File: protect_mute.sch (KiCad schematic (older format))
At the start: 40 parts, among them K1 G5LE-1, K2 G5LE-1, Q1 BC546, Q2 BC556, Q3 BC546, Q4 BD140

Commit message: Opened on home office computer. Some rescue and lib conversion happened. Need to confirm no changes on work laptop.
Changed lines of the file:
@@
 EESchema Schematic File Version 4
-LIBS:AAMB-cache
 EELAYER 30 0
 EELAYER END
@@
 	1650 2925 1550 2925
 $Comp
-L Power-amp:+35V #PWR04
+L AAMB-rescue:+35V-Power-amp #PWR04
 U 1 1 5E273D13
 P 1800 1525

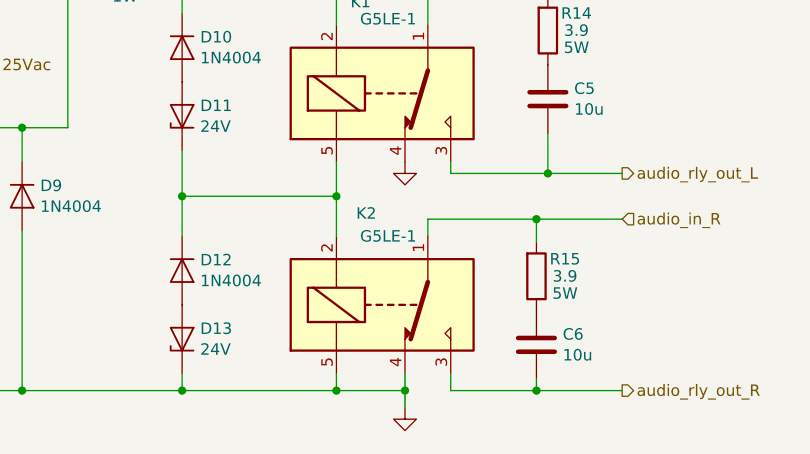
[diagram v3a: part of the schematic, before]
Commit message: Fixed several DRC errors. Tied audoi input returns to GND. Added Switch logic.
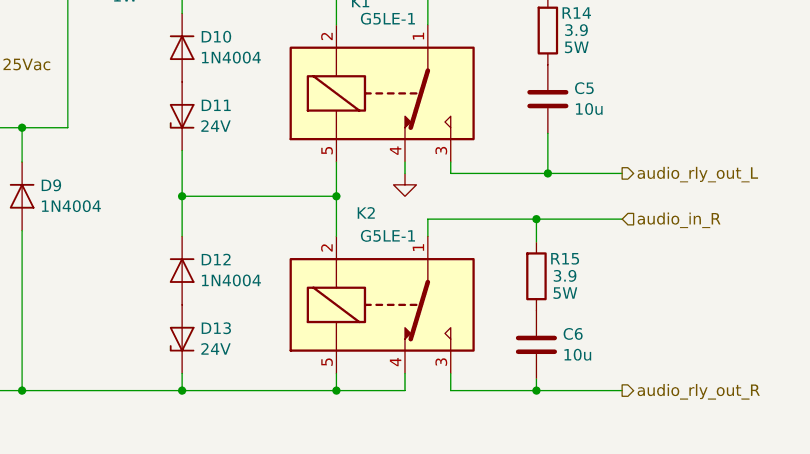
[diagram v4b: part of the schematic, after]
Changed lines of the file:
@@
 EESchema Schematic File Version 4
+LIBS:AAMB-cache
 EELAYER 30 0
 EELAYER END
@@
 L power:GND #PWR05
 U 1 1 5E3BFF33
-P 7400 3125
-F 0 "#PWR05" H 7400 2875 50  0001 C CNN
-F 1 "GND" H 7500 3000 50  0001 C CNN
-F 2 "" H 7400 3125 50  0001 C CNN
-F 3 "" H 7400 3125 50  0001 C CNN
-	1    7400 3125
+P 7400 3175
+F 0 "#PWR05" H 7400 2925 50  0001 C CNN
+F 1 "GND" H 7500 3050 50  0001 C CNN
+F 2 "" H 7400 3175 50  0001 C CNN
+F 3 "" H 7400 3175 50  0001 C CNN
+	1    7400 3175
 	1    0    0    -1
 $EndComp
@@
 	6325 2300 6425 2300
 Connection ~ 6425 2300
-$Comp
-L power:GND #PWR06
-U 1 1 5E3E6C3E
-P 7400 4200
-F 0 "#PWR06" H 7400 3950 50  0001 C CNN
-F 1 "GND" H 7475 4050 50  0001 C CNN
-F 2 "" H 7400 4200 50  0001 C CNN
-F 3 "" H 7400 4200 50  0001 C CNN
-	1    7400 4200
-	1    0    0    -1
-$EndComp
-Connection ~ 7400 4125
-Wire Wire Line
-	7400 4200 7400 4125
 Wire Wire Line
 	7600 3125 7600 3175
@@
 Text Label 6625 2300 0    50   ~ 0
 RLY+_L
+Wire Wire Line
+	7400 3175 7400 3125
 $EndSCHEMATC

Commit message: Schecmatic cleanup.
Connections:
- net RLY_-L_+R: now reaches D11.1 (K), D12.1 (K), K1.5, K2.2
- net RLY+_L renamed RLY_+L
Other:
- moved on the sheet: C1, C2, C3, C4, C5, C6, D1, D10, D11, D12, D13, D2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

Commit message: Cleaning up user configs.
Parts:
- C1, C2, C5, C6: footprint (none) -> Capacitor_SMD:C_1206_3216Metric_Pad1.42x1.75mm_HandSolder; DigiKey (none) -> https://www.digikey.com/product-detail/en/murata-electronic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
- C3, C4: footprint (none) -> Capacitor_THT:CP_Radial_D5.0mm_P2.00mm
- D11, D13: footprint (none) -> Diode_SMD:D_SMA
- R1, R10, R11, R12, R2, R3, R4, R5, R6, R7, R8, R9: footprint (none) -> Resistor_SMD:R_0603_1608Metric_Pad1.05x0.95mm_HandSolder
- R13: DigiKey (none) -> https://www.digikey.com/product-detail/en/yageo/FMP100JR-52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
- R14, R15: DigiKey (none) -> https://www.digikey.com/product-detail/en/vishay-bc-compone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
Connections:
- net audio_rly_out_L: now also C6.2; no longer C5.2
- net audio_rly_out_R: now also C5.2; no longer C6.2
- net at R15.1: now also C5.1; no longer C6.1
- net at R14.1: now also C6.1; no longer C5.1
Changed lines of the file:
@@
 F 0 "C4" H 5868 4746 50  0000 L CNN
 F 1 "1u" H 5868 4655 50  0000 L CNN
-F 2 "" H 5788 4550 50  0001 C CNN
+F 2 "Capacitor_THT:CP_Radial_D5.0mm_P2.00mm" H 5788 4550 50  0001 C CNN
 F 3 "~" H 5750 4700 50  0001 C CNN
 	1    5750 4700
@@
 F 0 "R12" V 5743 3525 50  0000 C CNN
 F 1 "100k" V 5834 3525 50  0000 C CNN
-F 2 "" V 5880 3525 50  0001 C CNN
+F 2 "Resistor_SMD:R_0603_1608Metric_Pad1.05x0.95mm_HandSolder" V 5880 3525 50  0001 C CNN
 F 3 "~" H 5950 3525 50  0001 C CNN
 	1    5950 3525
@@
 F 0 "R11" H 5370 4171 50  0000 L CNN
 F 1 "10k" H 5370 4080 50  0000 L CNN
-F 2 "" V 5230 4125 50  0001 C CNN
+F 2 "Resistor_SMD:R_0603_1608Metric_Pad1.05x0.95mm_HandSolder" V 5230 4125 50  0001 C CNN
 F 3 "~" H 5300 4125 50  0001 C CNN
 	1    5300 4125
@@
 F 0 "R10" V 4818 4425 50  0000 C CNN
 F 1 "10k" V 4909 4425 50  0000 C CNN
-F 2 "" V 4955 4425 50  0001 C CNN
+F 2 "Resistor_SMD:R_0603_1608Metric_Pad1.05x0.95mm_HandSolder" V 4955 4425 50  0001 C CNN
 F 3 "~" H 5025 4425 50  0001 C CNN
 	1    5025 4425
@@
 F 0 "R9" H 4480 3504 50  0000 R CNN
 F 1 "10k" H 4480 3595 50  0000 R CNN
-F 2 "" V 4480 3550 50  0001 C CNN
+F 2 "Resistor_SMD:R_0603_1608Metric_Pad1.05x0.95mm_HandSolder" V 4480 3550 50  0001 C CNN
 F 3 "~" H 4550 3550 50  0001 C CNN
 	1    4550 3550
@@
 F 0 "R8" H 3855 3504 50  0000 R CNN
 F 1 "100k" H 3855 3595 50  0000 R CNN
-F 2 "" V 3855 3550 50  0001 C CNN
+F 2 "Resistor_SMD:R_0603_1608Metric_Pad1.05x0.95mm_HandSolder" V 3855 3550 50  0001 C CNN
 F 3 "~" H 3925 3550 50  0001 C CNN
 	1    3925 3550
@@
 F 0 "R5" H 3330 3504 50  0000 R CNN
 F 1 "22k" H 3330 3595 50  0000 R CNN
-F 2 "" V 3330 3550 50  0001 C CNN
+F 2 "Resistor_SMD:R_0603_1608Metric_Pad1.05x0.95mm_HandSolder" V 3330 3550 50  0001 C CNN
 F 3 "~" H 3400 3550 50  0001 C CNN
 	1    3400 3550
@@
 F 0 "R4" H 3005 2679 50  0000 R CNN
 F 1 "100k" H 3005 2770 50  0000 R CNN
-F 2 "" V 3005 2725 50  0001 C CNN
+F 2 "Resistor_SMD:R_0603_1608Metric_Pad1.05x0.95mm_HandSolder" V 3005 2725 50  0001 C CNN
 F 3 "~" H 3075 2725 50  0001 C CNN
 	1    3075 2725
@@
 F 0 "R7" H 3855 2679 50  0000 R CNN
 F 1 "100k" H 3855 2770 50  0000 R CNN
-F 2 "" V 3855 2725 50  0001 C CNN
+F 2 "Resistor_SMD:R_0603_1608Metric_Pad1.05x0.95mm_HandSolder" V 3855 2725 50  0001 C CNN
 F 3 "~" H 3925 2725 50  0001 C CNN
 	1    3925 2725
@@
 F 0 "R6" H 3505 4679 50  0000 R CNN
 F 1 "22k" H 3505 4770 50  0000 R CNN
-F 2 "" V 3505 4725 50  0001 C CNN
+F 2 "Resistor_SMD:R_0603_1608Metric_Pad1.05x0.95mm_HandSolder" V 3505 4725 50  0001 C CNN
 F 3 "~" H 3575 4725 50  0001 C CNN
 	1    3575 4725
@@
 F 0 "R1" V 2182 3750 50  0000 C CNN
 F 1 "100k" V 2091 3750 50  0000 C CNN
-F 2 "" V 1905 3750 50  0001 C CNN
+F 2 "Resistor_SMD:R_0603_1608Metric_Pad1.05x0.95mm_HandSolder" V 1905 3750 50  0001 C CNN
 F 3 "~" H 1975 3750 50  0001 C CNN
 	1    1975 3750
@@
 F 0 "R2" V 2182 4500 50  0000 C CNN
 F 1 "100k" V 2091 4500 50  0000 C CNN
-F 2 "" V 1905 4500 50  0001 C CNN
+F 2 "Resistor_SMD:R_0603_1608Metric_Pad1.05x0.95mm_HandSolder" V 1905 4500 50  0001 C CNN
 F 3 "~" H 1975 4500 50  0001 C CNN
 	1    1975 4500
@@
 F 0 "R3" V 2800 2450 50  0000 C CNN
 F 1 "10" V 2600 2450 50  0000 C CNN
-F 2 "" V 2630 2450 50  0001 C CNN
+F 2 "Resistor_SMD:R_0603_1608Metric_Pad1.05x0.95mm_HandSolder" V 2630 2450 50  0001 C CNN
 F 3 "~" H 2700 2450 50  0001 C CNN
 	1    2700 2450
@@
 F 0 "C3" H 3193 3121 50  0000 L CNN
 F 1 "10u" H 3193 3030 50  0000 L CNN
-F 2 "" H 3113 2925 50  0001 C CNN
+F 2 "Capacitor_THT:CP_Radial_D5.0mm_P2.00mm" H 3113 2925 50  0001 C CNN
 F 3 "~" H 3075 3075 50  0001 C CNN
 	1    3075 3075
-	1    0    0    -1
-$EndComp
-$Comp
-L Device:C C1
-U 1 1 5E2701CA
-P 2225 4075
-F 0 "C1" H 2340 4121 50  0000 L CNN
-F 1 "10u" H 2340 4030 50  0000 L CNN
-F 2 "" H 2263 3925 50  0001 C CNN
-F 3 "~" H 2225 4075 50  0001 C CNN
-	1    2225 4075
-	1    0    0    -1
-$EndComp
-$Comp
-L Device:C C2
-U 1 1 5E270780
-P 2225 4725
-F 0 "C2" H 2340 4771 50  0000 L CNN
-F 1 "10u" H 2340 4680 50  0000 L CNN
-F 2 "" H 2263 4575 50  0001 C CNN
-F 3 "~" H 2225 4725 50  0001 C CNN
-	1    2225 4725
 	1    0    0    -1
 $EndComp
@@
 F 1 "150" V 6750 3125 50  0000 C CNN
 F 2 "Resistor_THT:R_Axial_DIN0207_L6.3mm_D2.5mm_P7.62mm_Horizontal" V 6680 3125 50  0001 C CNN
-F 3 "https://www.digikey.com/product-detail/en/yageo/FMP100JR-52-150R/150WTR-ND/2058579" H 6750 3125 50  0001 C CNN
+F 3 "" H 6750 3125 50  0001 C CNN
 F 4 "1W" V 6650 3125 50  0000 C CNN "Power"
+F 5 "https://www.digikey.com/product-detail/en/yageo/FMP100JR-52-150R/150WTR-ND/2058579" H 6750 3125 50  0001 C CNN "DigiKey"
 	1    6750 3125
 	0    1    -1   0
@@
 F 0 "D11" V 7046 3671 50  0000 R CNN
 F 1 "24V" V 6955 3671 50  0000 R CNN
-F 2 "" H 7000 3750 50  0001 C CNN
+F 2 "Diode_SMD:D_SMA" H 7000 3750 50  0001 C CNN
 F 3 "~" H 7000 3750 50  0001 C CNN
 	1    7000 3750
@@
 F 0 "D13" V 7046 4646 50  0000 R CNN
 F 1 "24V" V 6955 4646 50  0000 R CNN
-F 2 "" H 7000 4725 50  0001 C CNN
+F 2 "Diode_SMD:D_SMA" H 7000 4725 50  0001 C CNN
 F 3 "~" H 7000 4725 50  0001 C CNN
 	1    7000 4725
@@
 F 1 "3.9" H 8675 4450 50  0000 C CNN
 F 2 "Resistor_THT:R_Axial_Power_L25.0mm_W9.0mm_P10.16mm_Vertical" V 8480 4450 50  0001 C CNN
-F 3 "https://www.digikey.com/product-detail/en/vishay-bc-components/PAC500003908FAC000/PPC5D3.9TB-ND/595237" H 8550 4450 50  0001 C CNN
+F 3 "" H 8550 4450 50  0001 C CNN
 F 4 "5W" H 8675 4525 50  0000 C CNN "Power"
+F 5 "https://www.digikey.com/product-detail/en/vishay-bc-components/PAC500003908FAC000/PPC5D3.9TB-ND/595237" H 8550 4450 50  0001 C CNN "DigiKey"
 	1    8550 4450
 	1    0    0    1
@@
 F 1 "3.9" H 8725 3375 50  0000 C CNN
 F 2 "Resistor_THT:R_Axial_Power_L25.0mm_W9.0mm_P10.16mm_Vertical" V 8530 3375 50  0001 C CNN
-F 3 "https://www.digikey.com/product-detail/en/vishay-bc-components/PAC500003908FAC000/PPC5D3.9TB-ND/595237" H 8600 3375 50  0001 C CNN
+F 3 "" H 8600 3375 50  0001 C CNN
 F 4 "5W" H 8725 3450 50  0000 C CNN "Power"
+F 5 "https://www.digikey.com/product-detail/en/vishay-bc-components/PAC500003908FAC000/PPC5D3.9TB-ND/595237" H 8600 3375 50  0001 C CNN "DigiKey"
 	1    8600 3375
 	1    0    0    1
-$EndComp
-$Comp
-L Device:C C5
-U 1 1 5E37BBDD
-P 8600 3675
-F 0 "C5" H 8715 3721 50  0000 L CNN
-F 1 "10u" H 8715 3630 50  0000 L CNN
-F 2 "" H 8638 3525 50  0001 C CNN
-F 3 "~" H 8600 3675 50  0001 C CNN
-	1    8600 3675
-	1    0    0    -1
-$EndComp
-$Comp
-L Device:C C6
-U 1 1 5E37C2E4
-P 8550 4750
-F 0 "C6" H 8665 4796 50  0000 L CNN
-F 1 "10u" H 8665 4705 50  0000 L CNN
-F 2 "" H 8588 4600 50  0001 C CNN
-F 3 "~" H 8550 4750 50  0001 C CNN
-	1    8550 4750
-	1    0    0    -1
 $EndComp
 $Comp
@@
 Wire Wire Line
 	6250 3425 6250 3525
+$Comp
+L Device:C C2
+U 1 1 5E6DF6E6
+P 2225 4725
+F 0 "C2" H 2340 4771 50  0000 L CNN
+F 1 "10u" H 2340 4680 50  0000 L CNN
+F 2 "Capacitor_SMD:C_1206_3216Metric_Pad1.42x1.75mm_HandSolder" H 2263 4575 50  0001 C CNN
+F 3 "https://search.murata.co.jp/Ceramy/image/img/A01X/G101/ENG/GRT31CR61H106KE01-01.pdf" H 2225 4725 50  0001 C CNN
+F 4 "https://www.digikey.com/product-detail/en/murata-electronics/GRT31CR61H106KE01L/490-12456-1-ND/5417157" H 2225 4725 50  0001 C CNN "DigiKey"
+	1    2225 4725
+	1    0    0    -1
+$EndComp
+$Comp
+L Device:C C6
+U 1 1 5E6DFBAF
+P 8600 3675
+F 0 "C6" H 8715 3721 50  0000 L CNN
+F 1 "10u" H 8715 3630 50  0000 L CNN
+F 2 "Capacitor_SMD:C_1206_3216Metric_Pad1.42x1.75mm_HandSolder" H 8638 3525 50  0001 C CNN
+F 3 "https://search.murata.co.jp/Ceramy/image/img/A01X/G101/ENG/GRT31CR61H106KE01-01.pdf" H 8600 3675 50  0001 C CNN
+F 4 "https://www.digikey.com/product-detail/en/murata-electronics/GRT31CR61H106KE01L/490-12456-1-ND/5417157" H 8600 3675 50  0001 C CNN "DigiKey"
+	1    8600 3675
+	1    0    0    -1
+$EndComp
+$Comp
+L Device:C C5
+U 1 1 5E6E012C
+P 8550 4750
+F 0 "C5" H 8665 4796 50  0000 L CNN
+F 1 "10u" H 8665 4705 50  0000 L CNN
+F 2 "Capacitor_SMD:C_1206_3216Metric_Pad1.42x1.75mm_HandSolder" H 8588 4600 50  0001 C CNN
+F 3 "https://search.murata.co.jp/Ceramy/image/img/A01X/G101/ENG/GRT31CR61H106KE01-01.pdf" H 8550 4750 50  0001 C CNN
+F 4 "https://www.digikey.com/product-detail/en/murata-electronics/GRT31CR61H106KE01L/490-12456-1-ND/5417157" H 8550 4750 50  0001 C CNN "DigiKey"
+	1    8550 4750
+	1    0    0    -1
+$EndComp
+$Comp
+L Device:C C1
+U 1 1 5E6E314D
+P 2225 4075
+F 0 "C1" H 2340 4121 50  0000 L CNN
+F 1 "10u" H 2340 4030 50  0000 L CNN
+F 2 "Capacitor_SMD:C_1206_3216Metric_Pad1.42x1.75mm_HandSolder" H 2263 3925 50  0001 C CNN
+F 3 "https://search.murata.co.jp/Ceramy/image/img/A01X/G101/ENG/GRT31CR61H106KE01-01.pdf" H 2225 4075 50  0001 C CNN
+F 4 "https://www.digikey.com/product-detail/en/murata-electronics/GRT31CR61H106KE01L/490-12456-1-ND/5417157" H 2225 4075 50  0001 C CNN "DigiKey"
+	1    2225 4075
+	1    0    0    -1
+$EndComp
 $EndSCHEMATC
